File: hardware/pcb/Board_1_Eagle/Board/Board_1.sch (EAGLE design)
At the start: 93 parts, among them IC1 MCP73831, IC2 LT1963EST-1.5, IC3 VUB300, IC5 WTV020SD-20S, J3 DEBUG_CONNECTOR, SW1 SW_TACT_SMD, SW2 SW_TACT_SMD, SW3 SW_TACT_SMD, SW4 SW_TACT_SMD, SW5 SW_TACT_SMD, SW6 SW_TACT_SMD, SW7 SW_TACT_SMD, X1 1751248, X2 1751248, X3 1751248, Y1 CRYSTAL.3.2X2.5MM

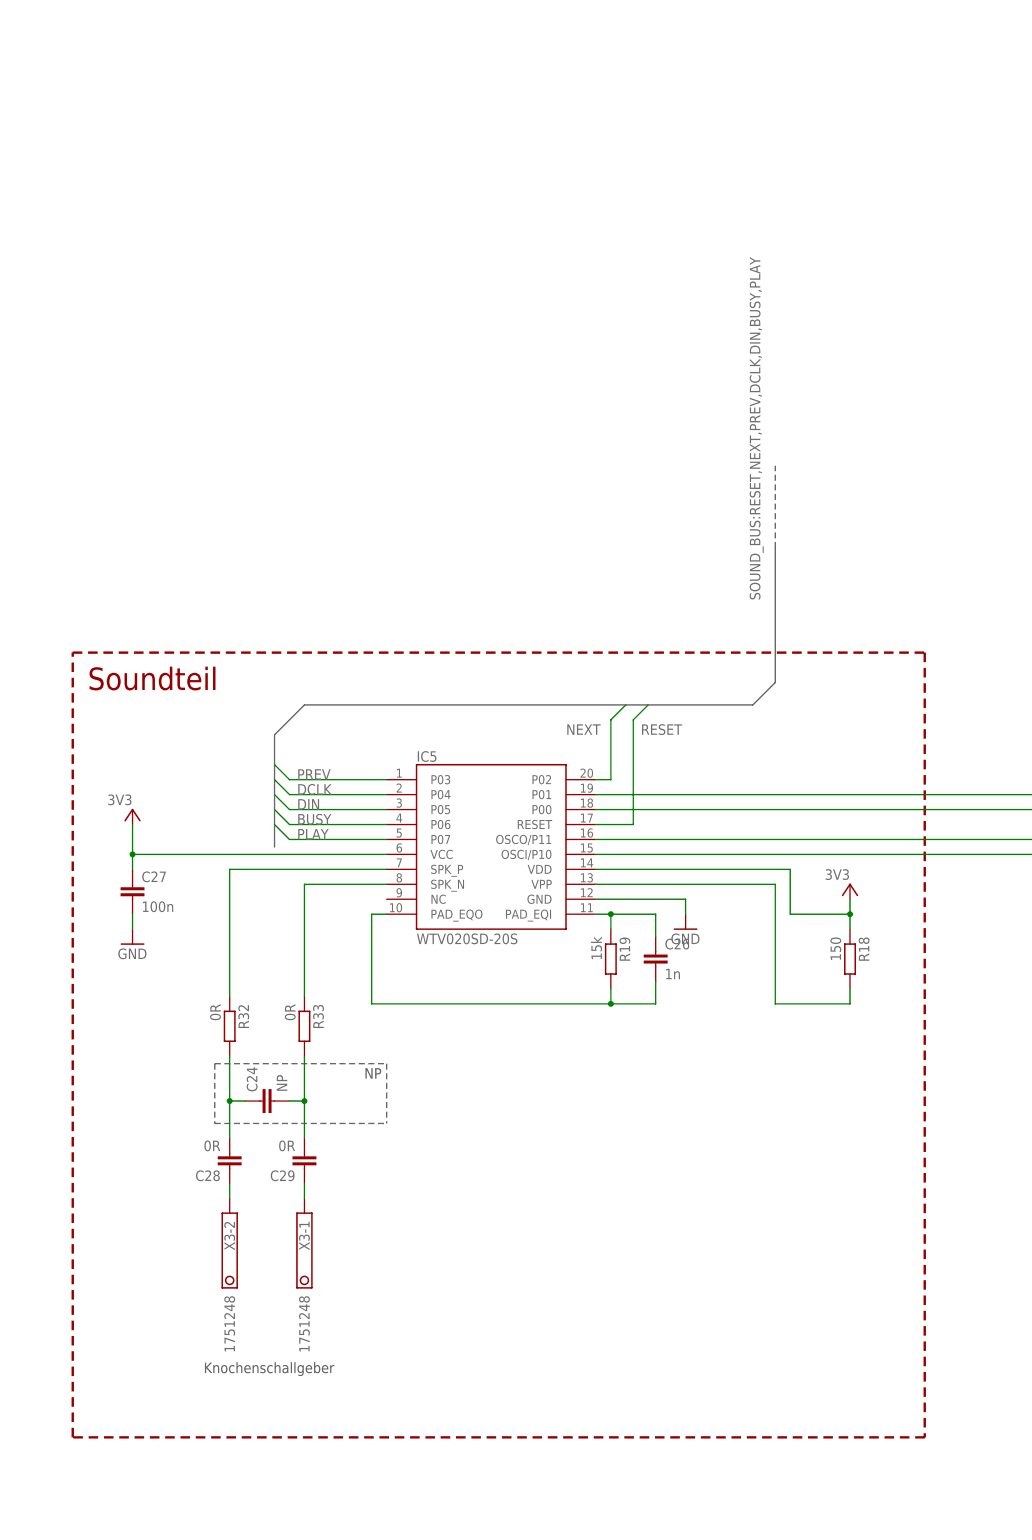
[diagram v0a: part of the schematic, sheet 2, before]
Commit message: Layout angepasst. Verstärker hinzugefügt
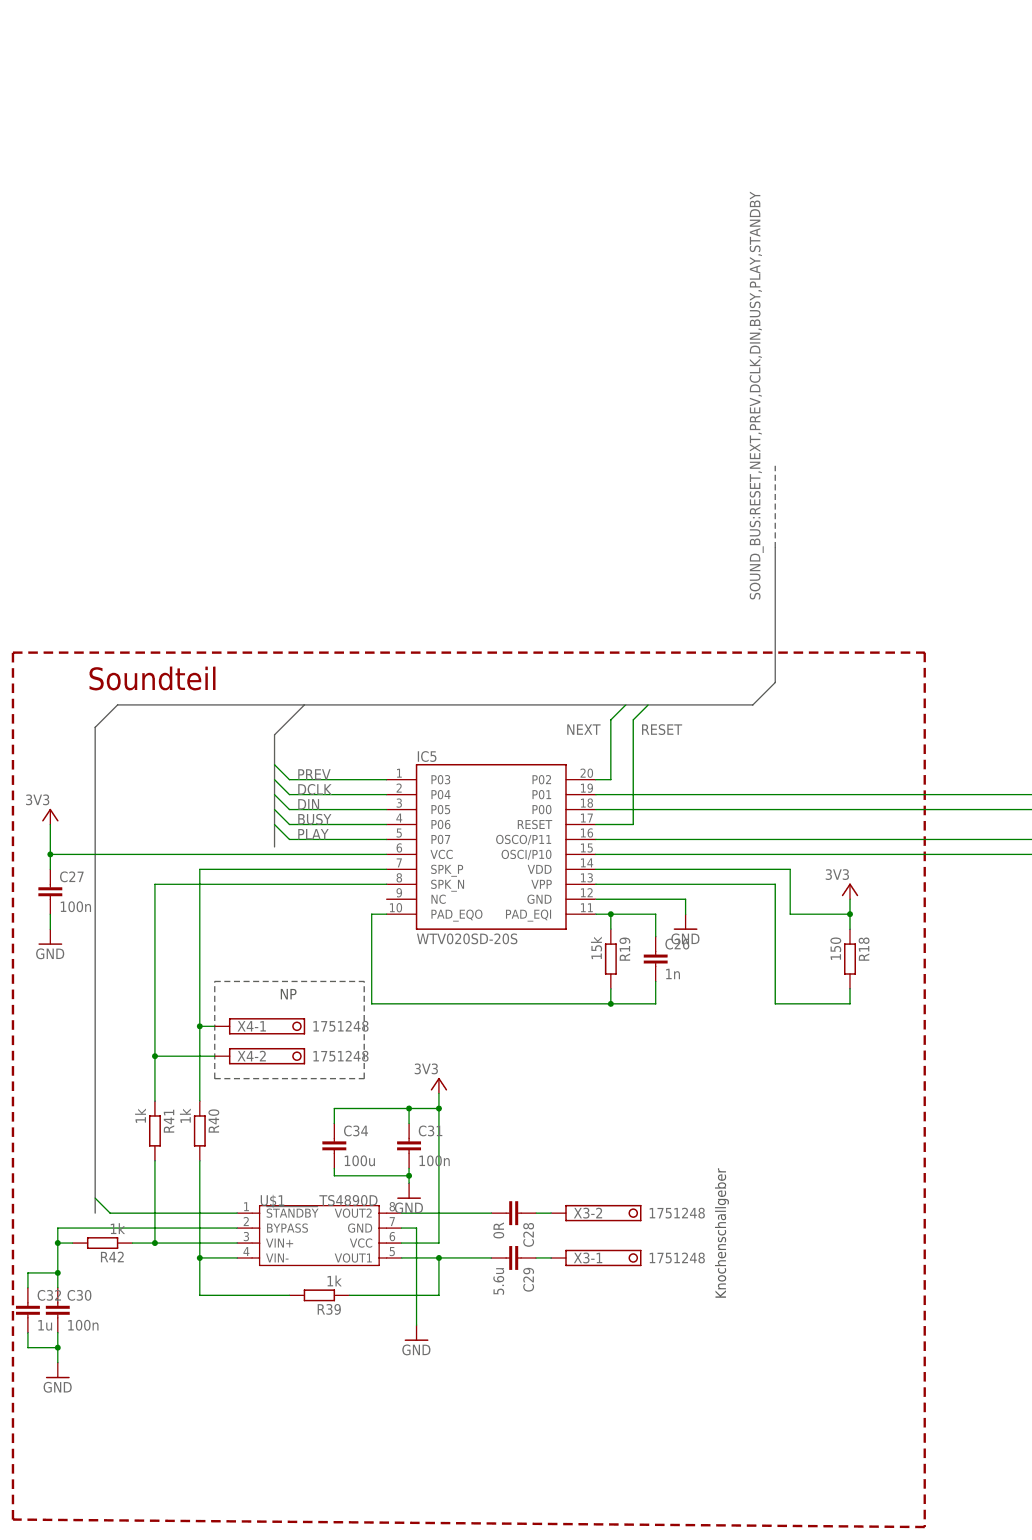
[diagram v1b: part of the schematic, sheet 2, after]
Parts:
- removed C24: NP, rcl:C-EUC0603
- removed R32, R33: 0R, resistor:R-EU_R0603
- added C30, C31: 100n, rcl:C-EUC0603
- added C32: 1u, rcl:C-EUC0805K
- added C34: 100u, rcl:C-EUC1206
- added R39, R40, R41, R42: 1k, resistor:R-EU_R0603
- added U$1: TS4890D, TI_IC:TS4890D
- added X4: 1751248, con-phoenix-350:1751248
- C29: value 0R -> 5.6u
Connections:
- removed net N$58: C24.2, C29.2, R33.2
- removed net N$59: C24.1, C28.2, R32.2
- new net N$11: C28.2, U$1.VOUT2
- new net N$12: C29.2, R39.1, U$1.VOUT1
- new net N$13: C30.1, C32.1, R42.2, U$1.BYPASS
- new net N$14: R39.2, R40.2, U$1.VIN-
- new net N$15: R41.2, R42.1, U$1.VIN+
- new net STANDBY: MOD1.P0.04/AIN2, U$1.!STANDBY
- net +3V3: now also C31.1, C34.1, U$1.VCC
- net GND: now also C30.2, C31.2, C32.2, C34.2, U$1.GND
- net SPK+: now also R40.1, X4-1.K; no longer R32.1
- net SPK-: now also R41.1, X4-2.K; no longer R33.1
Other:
- moved on the sheet: C27, C28, C29, X3-1, X3-2

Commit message: d
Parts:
- U$1: value TS4890D -> TS487ID
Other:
- moved on the sheet: C26, C27, C28, C29, C30, C31, C32, C34, IC5, R18, R19, R39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

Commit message: bla
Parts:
- renumbered GND to IC30
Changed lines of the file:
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@@
 <part name="R8" library="resistor" library_urn="urn:adsk.eagle:library:348" deviceset="R-EU_" device="R0603" package3d_urn="urn:adsk.eagle:package:26057/1" value="Ferit Bead"/>
 <part name="R9" library="resistor" library_urn="urn:adsk.eagle:library:348" deviceset="R-EU_" device="R0603" package3d_urn="urn:adsk.eagle:package:26057/1" value="Ferit Bead"/>
-<part name="GND" library="TS3a27" deviceset="TS3A27" device=""/>
+<part name="IC30" library="TS3a27" deviceset="TS3A27" device=""/>
 <part name="GND16" library="supply1" library_urn="urn:adsk.eagle:library:371" deviceset="GND" device=""/>
 <part name="IC5" library="SparkFun-DigitalIC" deviceset="WTV020SD" device="" value="WTV020SD-20S">
@@
 <instance part="FRAME2" gate="G$1" x="0" y="0"/>
 <instance part="FRAME2" gate="G$2" x="287.02" y="0"/>
-<instance part="GND" gate="G$1" x="218.44" y="173.99"/>
+<instance part="IC30" gate="G$1" x="218.44" y="173.99"/>
 <instance part="GND16" gate="1" x="325.12" y="92.71"/>
 <instance part="IC5" gate="G$1" x="80.01" y="140.97">
@@
 <wire x1="288.29" y1="120.65" x2="328.93" y2="120.65" width="0.1524" layer="91"/>
 <wire x1="288.29" y1="120.65" x2="288.29" y2="115.57" width="0.1524" layer="91"/>
-<pinref part="GND" gate="G$1" pin="COM5"/>
+<pinref part="IC30" gate="G$1" pin="COM5"/>
 <wire x1="288.29" y1="115.57" x2="238.76" y2="115.57" width="0.1524" layer="91"/>
 </segment>
@@
 <segment>
 <pinref part="IC5" gate="G$1" pin="P00"/>
-<pinref part="GND" gate="G$1" pin="NO2"/>
+<pinref part="IC30" gate="G$1" pin="NO2"/>
 <wire x1="113.03" y1="161.29" x2="127" y2="161.29" width="0.1524" layer="91"/>
 <wire x1="127" y1="161.29" x2="127" y2="168.91" width="0.1524" layer="91"/>
@@
 <wire x1="283.21" y1="130.81" x2="328.93" y2="130.81" width="0.1524" layer="91"/>
 <wire x1="283.21" y1="130.81" x2="283.21" y2="125.73" width="0.1524" layer="91"/>
-<pinref part="GND" gate="G$1" pin="COM3"/>
+<pinref part="IC30" gate="G$1" pin="COM3"/>
 <wire x1="283.21" y1="125.73" x2="238.76" y2="125.73" width="0.1524" layer="91"/>
 </segment>
@@
 <wire x1="255.27" y1="156.21" x2="255.27" y2="154.94" width="0.1524" layer="91"/>
 <junction x="255.27" y="156.21"/>
-<pinref part="GND" gate="G$1" pin="VCC"/>
+<pinref part="IC30" gate="G$1" pin="VCC"/>
 <wire x1="255.27" y1="156.21" x2="238.76" y2="156.21" width="0.1524" layer="91"/>
 </segment>
@@
 <pinref part="GND19" gate="1" pin="GND"/>
 <wire x1="205.74" y1="92.71" x2="205.74" y2="148.59" width="0.1524" layer="91"/>
-<pinref part="GND" gate="G$1" pin="NO1"/>
+<pinref part="IC30" gate="G$1" pin="NO1"/>
 <wire x1="205.74" y1="148.59" x2="205.74" y2="173.99" width="0.1524" layer="91"/>
 <wire x1="208.28" y1="173.99" x2="205.74" y2="173.99" width="0.1524" layer="91"/>
-<pinref part="GND" gate="G$1" pin="NO6"/>
+<pinref part="IC30" gate="G$1" pin="NO6"/>
 <wire x1="208.28" y1="148.59" x2="205.74" y2="148.59" width="0.1524" layer="91"/>
 <junction x="205.74" y="148.59"/>
@@
 </segment>
 <segment>
-<pinref part="GND" gate="G$1" pin="GND"/>
+<pinref part="IC30" gate="G$1" pin="GND"/>
 <wire x1="238.76" y1="151.13" x2="247.65" y2="151.13" width="0.1524" layer="91"/>
 <wire x1="247.65" y1="151.13" x2="247.65" y2="143.51" width="0.1524" layer="91"/>
@@
 <wire x1="285.75" y1="125.73" x2="328.93" y2="125.73" width="0.1524" layer="91"/>
 <wire x1="285.75" y1="125.73" x2="285.75" y2="120.65" width="0.1524" layer="91"/>
-<pinref part="GND" gate="G$1" pin="COM4"/>
+<pinref part="IC30" gate="G$1" pin="COM4"/>
 <wire x1="285.75" y1="120.65" x2="238.76" y2="120.65" width="0.1524" layer="91"/>
 </segment>
@@
 <wire x1="127" y1="158.75" x2="127" y2="156.21" width="0.1524" layer="91"/>
 <wire x1="127" y1="156.21" x2="113.03" y2="156.21" width="0.1524" layer="91"/>
-<pinref part="GND" gate="G$1" pin="NO4"/>
+<pinref part="IC30" gate="G$1" pin="NO4"/>
 </segment>
 </net>
@@
 <pinref part="IC5" gate="G$1" pin="OSCI/P10"/>
 <wire x1="113.03" y1="153.67" x2="208.28" y2="153.67" width="0.1524" layer="91"/>
-<pinref part="GND" gate="G$1" pin="NO5"/>
+<pinref part="IC30" gate="G$1" pin="NO5"/>
 </segment>
 </net>
@@
 <wire x1="280.67" y1="133.35" x2="328.93" y2="133.35" width="0.1524" layer="91"/>
 <wire x1="280.67" y1="133.35" x2="280.67" y2="130.81" width="0.1524" layer="91"/>
-<pinref part="GND" gate="G$1" pin="COM2"/>
+<pinref part="IC30" gate="G$1" pin="COM2"/>
 <wire x1="280.67" y1="130.81" x2="238.76" y2="130.81" width="0.1524" layer="91"/>
 </segment>
@@
 <pinref part="J2" gate="G$1" pin="DAT2"/>
 <wire x1="328.93" y1="135.89" x2="238.76" y2="135.89" width="0.1524" layer="91"/>
-<pinref part="GND" gate="G$1" pin="COM1"/>
+<pinref part="IC30" gate="G$1" pin="COM1"/>
 </segment>
 </net>
 <net name="N$44" class="0">
 <segment>
-<pinref part="GND" gate="G$1" pin="COM6"/>
+<pinref part="IC30" gate="G$1" pin="COM6"/>
 <wire x1="238.76" y1="110.49" x2="290.83" y2="110.49" width="0.1524" layer="91"/>
 <wire x1="290.83" y1="110.49" x2="290.83" y2="118.11" width="0.1524" layer="91"/>
@@
 <net name="D2" class="0">
 <segment>
-<pinref part="GND" gate="G$1" pin="NC1"/>
+<pinref part="IC30" gate="G$1" pin="NC1"/>
 <wire x1="208.28" y1="135.89" x2="193.04" y2="135.89" width="0.1524" layer="91"/>
 <wire x1="193.04" y1="135.89" x2="190.5" y2="138.43" width="0.1524" layer="91"/>
@@
 <net name="D3" class="0">
 <segment>
-<pinref part="GND" gate="G$1" pin="NC2"/>
+<pinref part="IC30" gate="G$1" pin="NC2"/>
 <wire x1="208.28" y1="130.81" x2="193.04" y2="130.81" width="0.1524" layer="91"/>
 <wire x1="193.04" y1="130.81" x2="190.5" y2="133.35" width="0.1524" layer="91"/>
@@
 <net name="CMD" class="0">
 <segment>
-<pinref part="GND" gate="G$1" pin="NC3"/>
+<pinref part="IC30" gate="G$1" pin="NC3"/>
 <wire x1="208.28" y1="125.73" x2="193.04" y2="125.73" width="0.1524" layer="91"/>
 <wire x1="193.04" y1="125.73" x2="190.5" y2="128.27" width="0.1524" layer="91"/>
@@
 <net name="CLK" class="0">
 <segment>
-<pinref part="GND" gate="G$1" pin="NC4"/>
+<pinref part="IC30" gate="G$1" pin="NC4"/>
 <wire x1="208.28" y1="120.65" x2="193.04" y2="120.65" width="0.1524" layer="91"/>
 <wire x1="193.04" y1="120.65" x2="190.5" y2="123.19" width="0.1524" layer="91"/>
@@
 <net name="D0" class="0">
 <segment>
-<pinref part="GND" gate="G$1" pin="NC5"/>
+<pinref part="IC30" gate="G$1" pin="NC5"/>
 <wire x1="208.28" y1="115.57" x2="193.04" y2="115.57" width="0.1524" layer="91"/>
 <wire x1="193.04" y1="115.57" x2="190.5" y2="118.11" width="0.1524" layer="91"/>
@@
 <wire x1="208.28" y1="110.49" x2="193.04" y2="110.49" width="0.1524" layer="91"/>
 <wire x1="193.04" y1="110.49" x2="190.5" y2="113.03" width="0.1524" layer="91"/>
-<pinref part="GND" gate="G$1" pin="NC6"/>
+<pinref part="IC30" gate="G$1" pin="NC6"/>
 <label x="194.31" y="111.76" size="1.778" layer="95"/>
 </segment>
@@
 <segment>
 <wire x1="252.73" y1="217.17" x2="250.19" y2="214.63" width="0.1524" layer="91"/>
-<pinref part="GND" gate="G$1" pin="IN1"/>
+<pinref part="IC30" gate="G$1" pin="IN1"/>
 <wire x1="238.76" y1="173.99" x2="241.3" y2="173.99" width="0.1524" layer="91"/>
 <wire x1="241.3" y1="173.99" x2="241.3" y2="168.91" width="0.1524" layer="91"/>
-<pinref part="GND" gate="G$1" pin="IN2"/>
+<pinref part="IC30" gate="G$1" pin="IN2"/>
 <wire x1="241.3" y1="168.91" x2="238.76" y2="168.91" width="0.1524" layer="91"/>
 <wire x1="241.3" y1="168.91" x2="250.19" y2="168.91" width="0.1524" layer="91"/>
@@
 <net name="N$47" class="0">
 <segment>
-<pinref part="GND" gate="G$1" pin="NC"/>
+<pinref part="IC30" gate="G$1" pin="NC"/>
 <wire x1="238.76" y1="143.51" x2="241.3" y2="143.51" width="0.1524" layer="91"/>
 </segment>
@@
 <segment>
 <wire x1="261.62" y1="217.17" x2="259.08" y2="214.63" width="0.1524" layer="91"/>
-<pinref part="GND" gate="G$1" pin="/EN"/>
+<pinref part="IC30" gate="G$1" pin="/EN"/>
 <wire x1="278.13" y1="163.83" x2="259.08" y2="163.83" width="0.1524" layer="91"/>
 <wire x1="259.08" y1="163.83" x2="238.76" y2="163.83" width="0.1524" layer="91"/>
@@
 <segment>
 <pinref part="IC5" gate="G$1" pin="P01"/>
-<pinref part="GND" gate="G$1" pin="NO3"/>
+<pinref part="IC30" gate="G$1" pin="NO3"/>
 <wire x1="113.03" y1="163.83" x2="208.28" y2="163.83" width="0.1524" layer="91"/>
 </segment>
